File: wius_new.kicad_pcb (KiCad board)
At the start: 6 copper layers, 54 x 28 mm, 132 parts, among them IC1 BQ24040DSQT, J2 52746-1271, J3 1040310811, J4 SS5-10-3.00-L-D-K-TR, J5 USB4745-03-A, J8 2, J9 U.FL, M1 MountingHole_Pad, M2 MountingHole_Pad, M3 MountingHole_Pad, M4 MountingHole_Pad, SW3 Button Switch SPST-No, SW4 Button Switch SPST-No, U1 TPS62840YBGR, U12 SN74LVC1T45DCK, U13 TXB0104RUT, U2 TXB0104RUT, U3 SiWG917Y, U4 FT232HPQ, U5 LSM6DSV, U6 SN74AXC4T774RSVR, U7 SOIC_clipProgSmall, U8 SN74AXC4T774RSVR, U9 PCAL6408AHK, Y1 SIT1552AI-JE-DCC-32.768E

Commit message: updated power routing
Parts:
- moved C33 5.74 mm to (166.3, 108.6)
- moved R27 5.74 mm to (166.2, 106.7)
- moved R33 1.67 mm to (160.7, 95.0)
- moved R24 1.42 mm to (162.6, 108.7)
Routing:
- net /IMU_SD/SPI_MCU.CS1: track 183.7 -> 9.08 mm
- net 3V3_VBUS: track 0.00 -> 156.5 mm
- net VIO: track 0.59 -> 116.0 mm
- net /MCU/SPI_FPGA.MOSI: track 43.8 -> 14.6 mm
- net 5V: track 7.18 -> 21.3 mm
- net VBATTERY: track 54.4 -> 65.0 mm
- net 1V8: track 0.00 -> 4.72 mm
- net /IMU_SD/SPI_MCU.SCK: track 14.6 -> 16.2 mm
- net Net-(U3C-GPIO_25): track 2.94 -> 1.85 mm

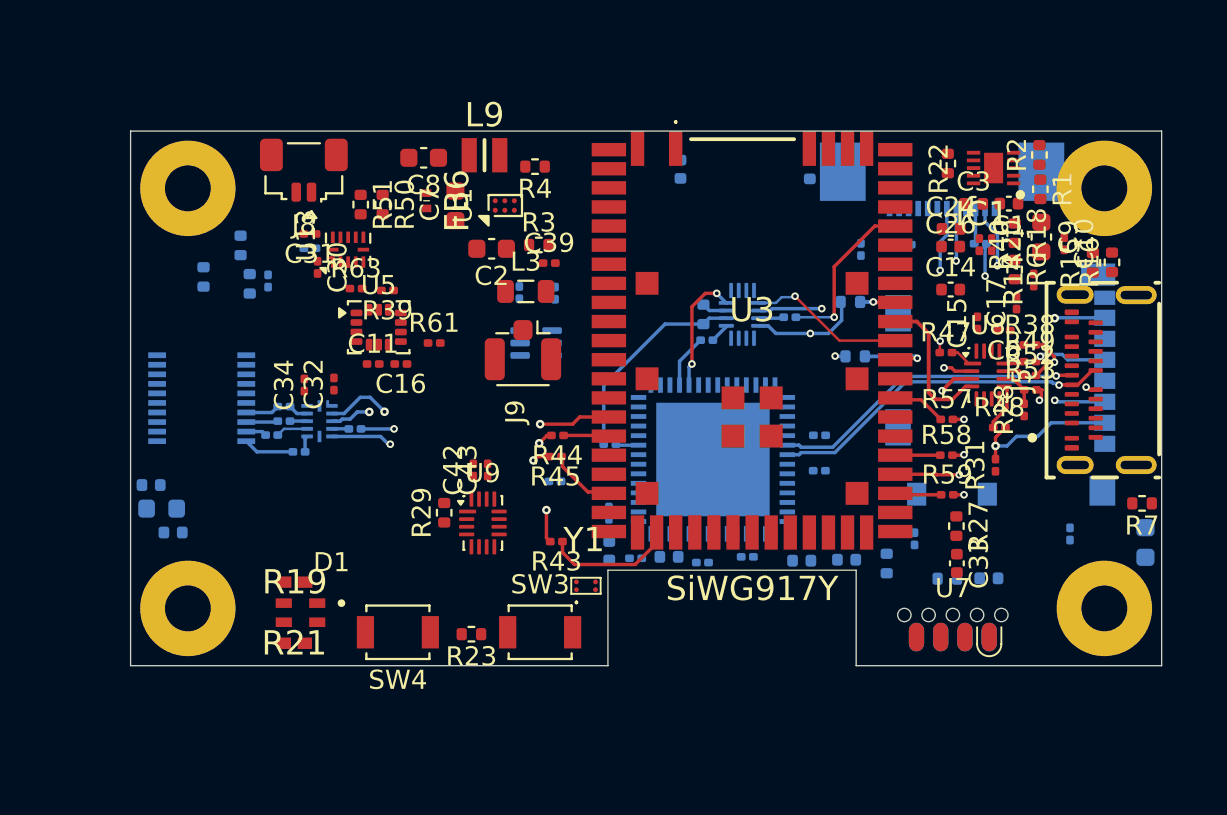
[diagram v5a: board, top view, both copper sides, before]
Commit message: initial power planes
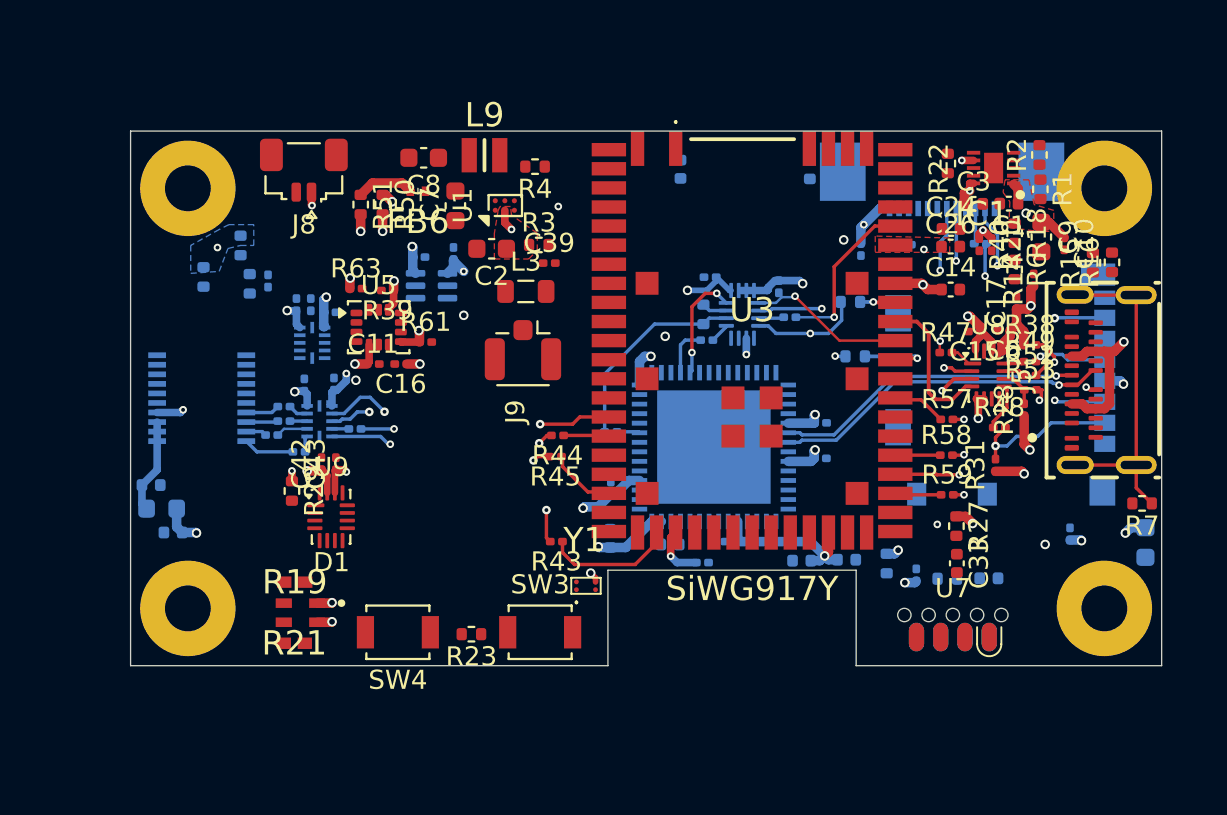
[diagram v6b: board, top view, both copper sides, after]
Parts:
- C30, C31, C32, C34, U13: moved to B.Cu
- moved C35 16.1 mm to (156.9, 94.2), turned to -90 degrees
- moved C36 13.4 mm to (153.3, 93.7), turned to 180 degrees
- moved R29 8.06 mm to (131.4, 104.8), turned to -90 degrees
- moved C42 7.96 mm to (133.0, 103.4)
- moved C43 7.96 mm to (133.8, 103.4)
- moved U9 7.96 mm to (133.5, 106.2)
- moved U12 6.24 mm to (138.8, 94.1)
- moved C37 5.71 mm to (139.9, 92.4)
- moved C38 5.58 mm to (138.1, 92.6), turned to 0 degrees
- moved U13 5.23 mm to (132.5, 97.1), turned to 180 degrees
- moved C31 3.77 mm to (131.7, 95.1), turned to 90 degrees
- moved R62 2.96 mm to (132.4, 95.1), turned to 90 degrees
- moved C30 2.44 mm to (133.4, 95.5), turned to 0 degrees
- moved R17 1.90 mm to (164.2, 109.2)
- moved C20 1.32 mm to (148.2, 104.7)
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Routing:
- net VIO: track 116.0 -> 203.1 mm, vias 0 -> 26
- net 3V3_VBUS: track 156.5 -> 192.1 mm, vias 0 -> 24
- net VBATTERY: track 65.0 -> 82.9 mm, vias 0 -> 8
- net Net-(J5-SHIELD): track 0.00 -> 17.7 mm
- net 5V: track 21.3 -> 32.7 mm, vias 0 -> 3
- net Net-(C114-Pad1): track 0.00 -> 4.96 mm
- net 1V8: track 4.72 -> 7.76 mm
- net /USB_FT232HPQ/SPI_FT232.CS: track 6.47 -> 5.79 mm
- added copper zone on In3.Cu, net 3V3_VBUS
- added copper zone on F.Cu, net 5V
- added copper zone on In3.Cu, net 5V
- added copper zone on B.Cu, net VBATTERY
- added copper zone on F.Cu, net VBATTERY
- added copper zone on In3.Cu, net VBATTERY
- added copper zone on F.Cu, net VIO
- added copper zone on In3.Cu, net VIO

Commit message: updated pcb
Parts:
- moved C35 3.79 mm to (153.2, 93.6), turned to 180 degrees
- moved C36 0.67 mm to (153.2, 94.3)
- moved R20 0.18 mm to (168.2, 91.8), turned to 90 degrees
- moved R40 0.16 mm to (167.4, 91.8), turned to 90 degrees
- moved R56 0.15 mm to (153.2, 97.1)
- turned R23 to 0 degrees
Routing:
- net 3V3_VBUS: track 192.1 -> 71.3 mm, vias 24 -> 25
- net VIO: track 203.1 -> 106.9 mm, vias 26 -> 28
- net VBATTERY: track 82.9 -> 8.73 mm, vias 8 -> 10
- net 5V: track 32.7 -> 13.7 mm, vias 3 -> 4
- net /MCU/FT_EN: track 0.00 -> 5.52 mm
- net 1V8: track 7.76 -> 3.03 mm
- net /MCU/INT_FFC: track 0.00 -> 1.49 mm, vias 0 -> 1
- net GND: track 0.00 -> 0.80 mm, vias 0 -> 6
- net /IMU_SD/SPI_MCU.SCK: track 16.2 -> 16.9 mm
- net /MCU/ULP_SSI.MOSI: track 15.7 -> 15.2 mm
- added copper zone on In1.Cu, net GND
- added copper zone on In4.Cu, net GND

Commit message: updated routing
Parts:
- moved R16 14.4 mm to (170.3, 106.7), turned to -90 degrees
- moved R15 13.8 mm to (169.2, 106.1), turned to -90 degrees
- moved R24 5.51 mm to (168.1, 107.8)
- moved C36 1.59 mm to (151.7, 94.7)
- moved C35 1.58 mm to (151.7, 93.9)
- moved R47 1.45 mm to (165.7, 99.0)
- moved R62 1.39 mm to (132.5, 93.7)
- moved C20 0.96 mm to (148.8, 104.0)
- moved C22 0.70 mm to (155.2, 107.5)
- moved U4 0.65 mm to (154.2, 102.5)
- moved C41 0.63 mm to (152.4, 108.3)
- moved C23 0.48 mm to (150.8, 107.7)
- moved C21 0.38 mm to (159.5, 103.1)
- moved C18 0.27 mm to (159.4, 101.3)
- turned R4 to 0 degrees
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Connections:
- R47 pad 2: Net-(U8-A1) -> Net-(U8-A3)
- R49 pad 1: Net-(U8-B3) -> Net-(U8-B1)
- U8 pad 1: Net-(U8-A1) -> /IMU_SD/SPI_MCU.SCK
- U8 pad 10: Net-(U8-B3) -> /IMU_SD/SPI_SD.MISO
- U8 pad 12: /IMU_SD/SPI_SD.MISO -> Net-(U8-B1)
- U8 pad 15: GND -> VIO
- U8 pad 3: /IMU_SD/SPI_MCU.SCK -> Net-(U8-A3)
- U8 pad 5: VIO -> GND
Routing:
- net /IMU_SD/I2C_IMU.SCL: track 0.00 -> 67.7 mm, vias 0 -> 5
- net /IMU_SD/I2C_IMU.SDA: track 0.00 -> 62.9 mm, vias 0 -> 5
- net /DEBUG, RESET & POC_IN, PROGRAMMING INTERFACE/SWD_MCU.SWO: track 0.00 -> 61.1 mm, vias 0 -> 4
- net /DEBUG, RESET & POC_IN, PROGRAMMING INTERFACE/UART_ULP.TX: track 0.00 -> 56.8 mm, vias 0 -> 2
- net /MCU/INT_FFC: track 1.49 -> 49.2 mm, vias 1 -> 4
- net /MCU/FPGA_EN: track 0.00 -> 45.2 mm, vias 0 -> 3
- net /MCU/CTRL_PWR.-5V: track 0.00 -> 43.5 mm, vias 0 -> 3
- net /MCU/CTRL_PWR.+HV: track 0.00 -> 40.7 mm, vias 0 -> 3
- net /MCU/CTRL_PWR.LVDS: track 0.00 -> 40.4 mm, vias 0 -> 4
- net /DEBUG, RESET & POC_IN, PROGRAMMING INTERFACE/SWD_MCU.SWCLK: track 0.00 -> 39.6 mm, vias 0 -> 3
- net /MCU/MCU_POWER_RF/Flash_IO_VDD: track 0.00 -> 39.5 mm, vias 0 -> 2
- net /DEBUG, RESET & POC_IN, PROGRAMMING INTERFACE/UART_ULP.RX: track 0.00 -> 39.4 mm, vias 0 -> 2
- net /DEBUG, RESET & POC_IN, PROGRAMMING INTERFACE/SWD_MCU.SWDIO: track 0.00 -> 36.1 mm, vias 0 -> 2
- net /MCU/MCU_POWER_RF/POC_IN: track 0.00 -> 34.2 mm, vias 0 -> 4
- net /USB_FT232HPQ/USB_CC2: track 0.00 -> 31.8 mm, vias 0 -> 3
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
